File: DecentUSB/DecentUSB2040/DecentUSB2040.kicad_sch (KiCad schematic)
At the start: 128 parts, among them J1 USB_B_Micro, J10 SM03B-SRSS-TB, J11 Conn_01x04, J2 Conn_01x08, J3 Conn_01x08, J5 Conn_02x09_Counter_Clockwise, J6 Conn_02x05_Odd_Even, J7 Conn_01x08, J8 Conn_01x03, J9 Conn_01x04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

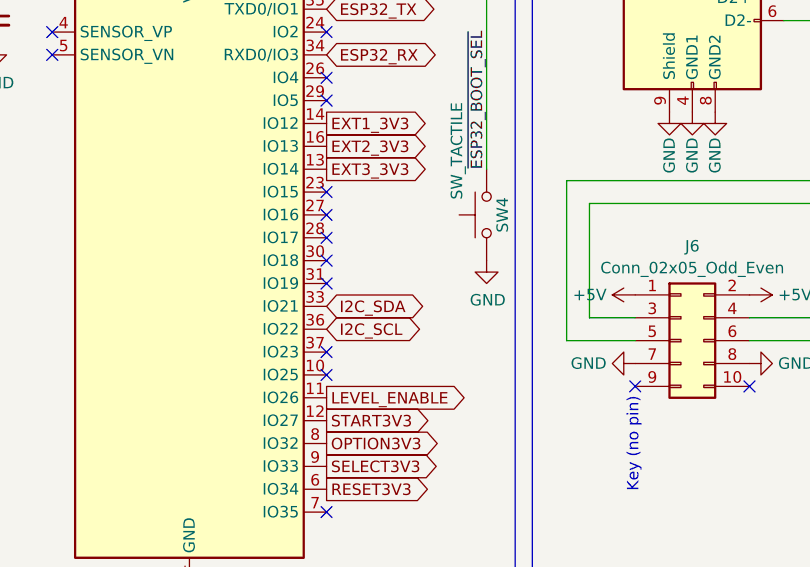
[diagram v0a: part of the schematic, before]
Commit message: DecentUSB Host 2040 rev. 3
Now using the already available RP2040 MCU
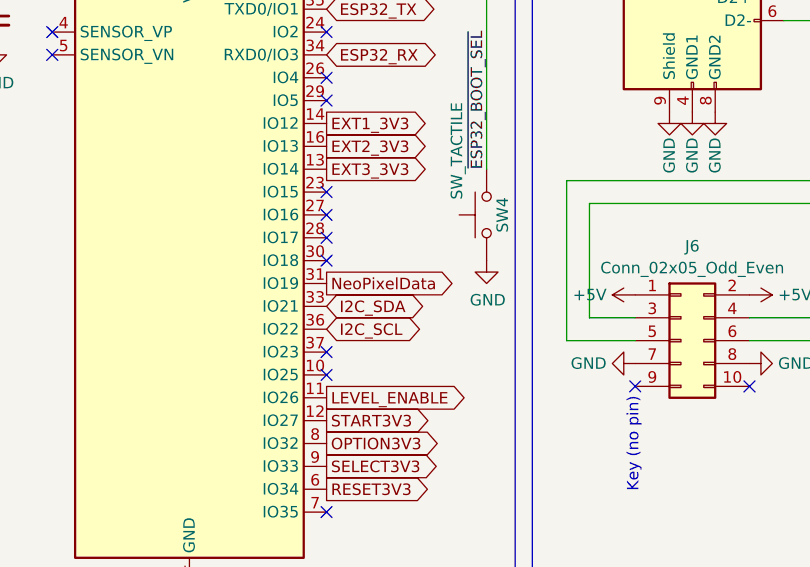
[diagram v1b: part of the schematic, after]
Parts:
- D2: footprint LED_SMD:LED_WS2812B_PLCC4_5.0x5.0mm_P3.2mm -> DecenTKL:WS2812C; JLCPCB Part # C5349953 -> C4154872
- J2, J3, J5, J6, J7, J9, R9, USB1-2: now left out of the parts list
- U1: JLCPCB Position Offset (none) -> 0,-0.8; JLCPCB Rotation Offset (none) -> 270
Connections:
- net NeoPixelData: now also U1.31 (IO19)
- no-connect marks 24 -> 23
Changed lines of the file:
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@@
 	)
 	(no_connect
-		(at 267.97 67.31)
-	)
-	(no_connect
 		(at 196.85 168.91)
 	)
@@
 		)
 	)
+	(global_label "NeoPixelData"
+		(shape output)
+		(at 267.97 67.31 0)
+		(fields_autoplaced yes)
+		(effects
+			(font
+				(size 1.27 1.27)
+			)
+			(justify left)
+		)
+		(property "Intersheetrefs" "${INTERSHEET_REFS}"
+			(at 283.4737 67.31 0)
+			(effects
+				(font
+					(size 1.27 1.27)
+				)
+				(justify left)
+				(hide yes)
+			)
+		)
+	)
 	(global_label "SIO:DATA_OUT3V3"
 		(shape output)
@@
 		(unit 1)
 		(exclude_from_sim no)
-		(in_bom yes)
+		(in_bom no)
 		(on_board yes)
 		(dnp no)
@@
 		(unit 1)
 		(exclude_from_sim no)
-		(in_bom yes)
+		(in_bom no)
 		(on_board yes)
 		(dnp no)
@@
 		(unit 1)
 		(exclude_from_sim no)
-		(in_bom yes)
+		(in_bom no)
 		(on_board yes)
 		(dnp no)
@@
 			)
 		)
-		(property "Footprint" "LED_SMD:LED_WS2812B_PLCC4_5.0x5.0mm_P3.2mm"
+		(property "Footprint" "DecenTKL:WS2812C"
 			(at 233.68 129.54 0)
 			(effects
@@
 			)
 		)
-		(property "JLCPCB Part #" "C5349953"
+		(property "JLCPCB Part #" "C4154872"
 			(at 232.41 121.92 0)
 			(effects
@@
 		(unit 1)
 		(exclude_from_sim no)
-		(in_bom yes)
+		(in_bom no)
 		(on_board yes)
 		(dnp no)
@@
 		(unit 1)
 		(exclude_from_sim no)
-		(in_bom yes)
+		(in_bom no)
 		(on_board yes)
 		(dnp no)
@@
 		(unit 1)
 		(exclude_from_sim no)
-		(in_bom yes)
+		(in_bom no)
 		(on_board yes)
 		(dnp no)
@@
 		(unit 1)
 		(exclude_from_sim no)
-		(in_bom yes)
+		(in_bom no)
 		(on_board yes)
 		(dnp yes)
@@
 			)
 		)
+		(property "JLCPCB Rotation Offset" "270"
+			(at 252.73 64.77 0)
+			(effects
+				(font
+					(size 1.27 1.27)
+				)
+				(hide yes)
+			)
+		)
+		(property "JLCPCB Position Offset" "0,-0.8"
+			(at 252.73 64.77 0)
+			(effects
+				(font
+					(size 1.27 1.27)
+				)
+				(hide yes)
+			)
+		)
 		(pin "3"
 		)
@@
 		(unit 1)
 		(exclude_from_sim no)
-		(in_bom yes)
+		(in_bom no)
 		(on_board yes)
 		(dnp no)

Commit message: Small production adjustment to DecentUSB 2040
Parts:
- J8: footprint Connector_JST:JST_SH_SM03B-SRSS-TB_1x03-1MP_P1.00mm_Horizontal -> Connector_JST:JST_SH_BM03B-SRSS-TB_1x03-1MP_P1.00mm_Vertical
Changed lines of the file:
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@@
 			)
 		)
-		(property "Footprint" "Connector_JST:JST_SH_SM03B-SRSS-TB_1x03-1MP_P1.00mm_Horizontal"
+		(property "Footprint" "Connector_JST:JST_SH_BM03B-SRSS-TB_1x03-1MP_P1.00mm_Vertical"
 			(at 248.92 134.62 0)
 			(effects

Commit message: DecentUSB 2040 adjustments
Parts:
- J8: JLCPCB Rotation Offset (none) -> 180
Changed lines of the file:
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@@
+			)
+		)
+		(property "JLCPCB Rotation Offset" "180"
+			(at 248.92 134.62 0)
+			(effects
+				(font
+					(size 1.27 1.27)
+				)
+				(hide yes)
 			)
 		)
